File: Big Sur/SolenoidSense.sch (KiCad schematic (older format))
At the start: 12 parts, among them U4 ACS70331EOLCTR, U5 ACS70331EOLCTR, U6 ACS70331EOLCTR, U7 ACS70331EOLCTR, U8 ACS70331EOLCTR, U9 ACS70331EOLCTR

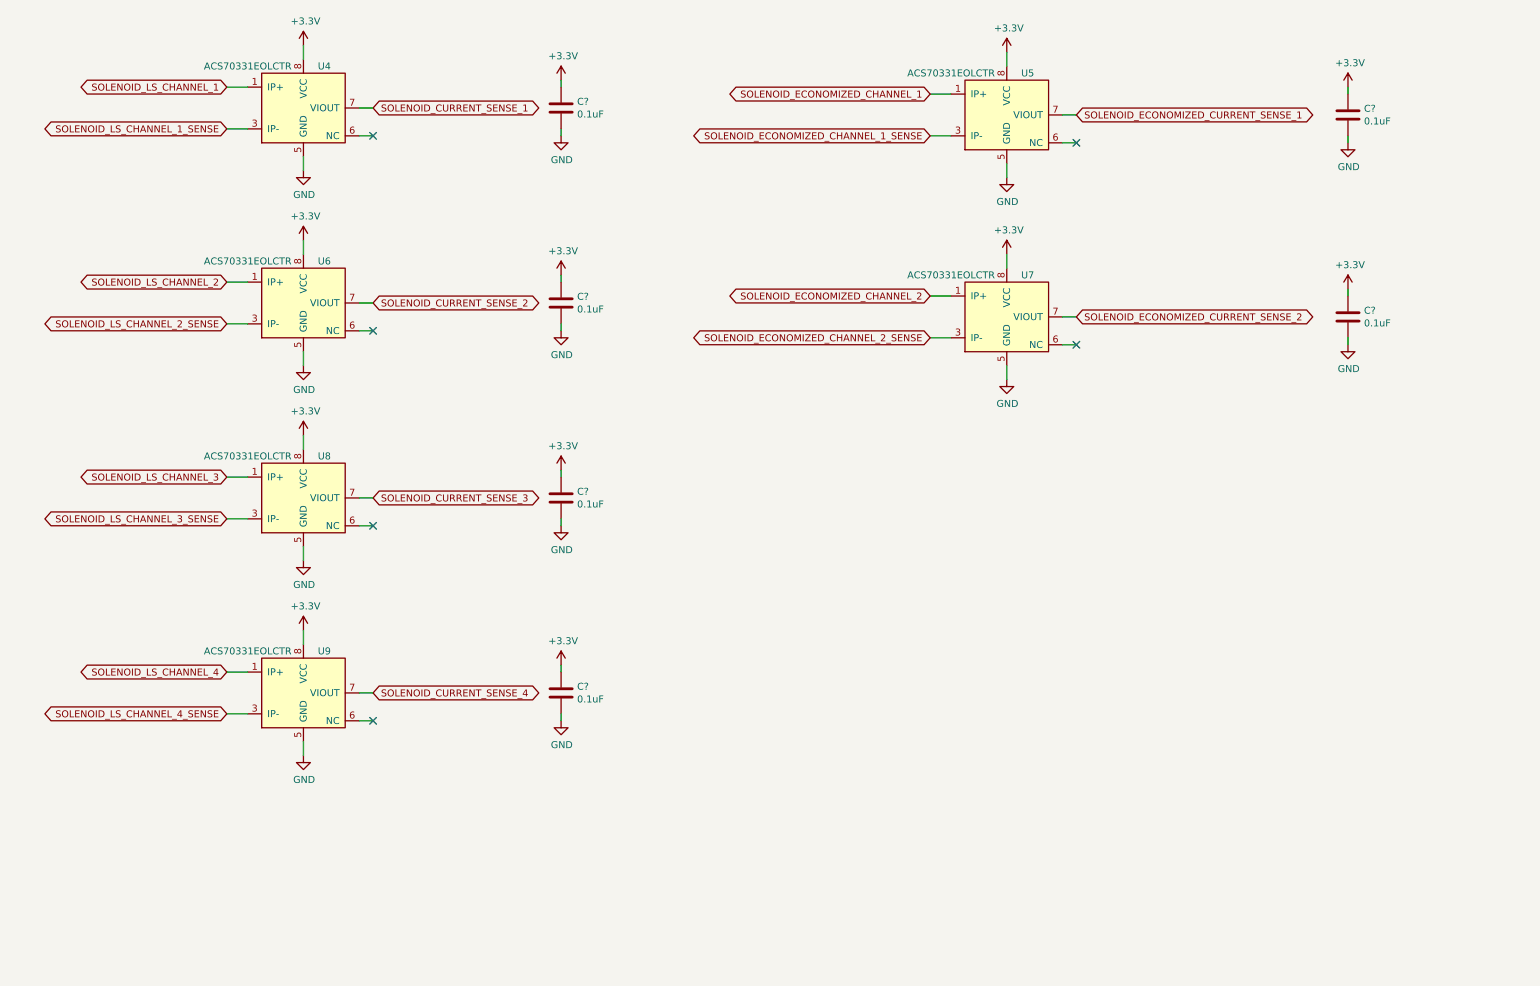
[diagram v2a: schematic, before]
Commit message: Schematics Complete
Still need to spec resistors, and XT30s, then should be ready for layout and routing.
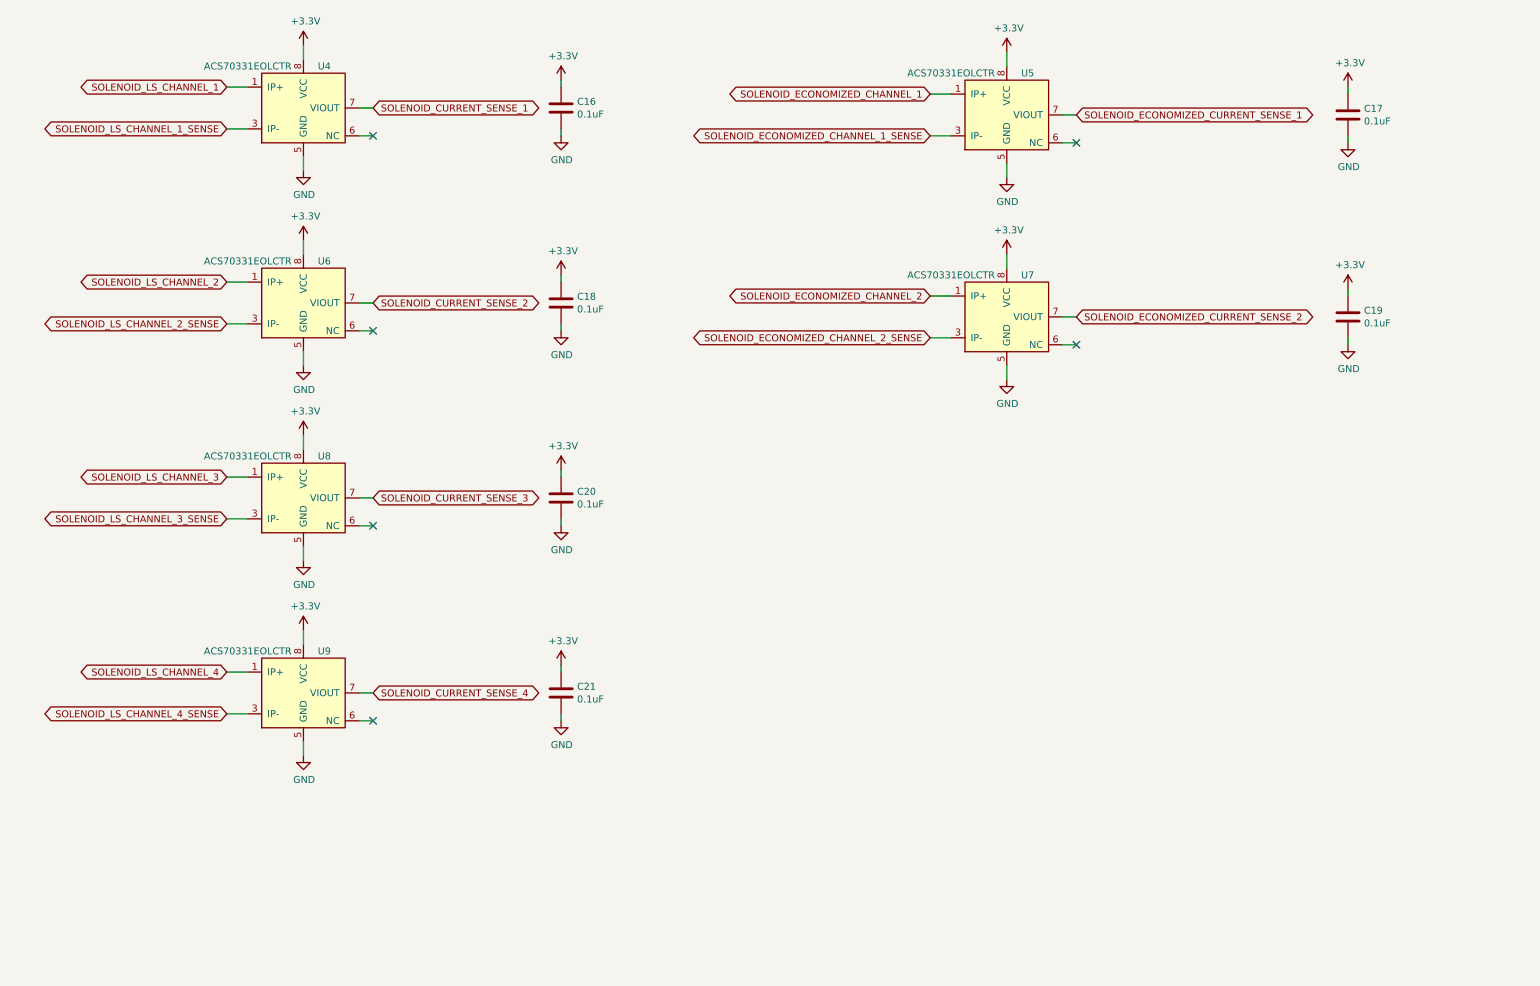
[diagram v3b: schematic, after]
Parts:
- gave numbers to parts that had none: 6
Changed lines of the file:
@@
 $EndDescr
 $Comp
-L power:+3.3V #PWR045
+L power:+3.3V #PWR046
 U 1 1 5DA28059
 P 2450 800
-F 0 "#PWR045" H 2450 650 50  0001 C CNN
+F 0 "#PWR046" H 2450 650 50  0001 C CNN
 F 1 "+3.3V" H 2465 973 50  0000 C CNN
 F 2 "" H 2450 800 50  0001 C CNN
@@
 	2450 900  2450 800
 $Comp
-L power:GND #PWR051
+L power:GND #PWR052
 U 1 1 5DA3AF60
 P 2450 1700
-F 0 "#PWR051" H 2450 1450 50  0001 C CNN
+F 0 "#PWR052" H 2450 1450 50  0001 C CNN
 F 1 "GND" H 2455 1527 50  0000 C CNN
 F 2 "" H 2450 1700 50  0001 C CNN
@@
 $EndComp
 $Comp
-L power:+3.3V #PWR047
+L power:+3.3V #PWR048
 U 1 1 5DA3EB08
 P 4300 1050
-F 0 "#PWR047" H 4300 900 50  0001 C CNN
+F 0 "#PWR048" H 4300 900 50  0001 C CNN
 F 1 "+3.3V" H 4315 1223 50  0000 C CNN
 F 2 "" H 4300 1050 50  0001 C CNN
@@
 $EndComp
 $Comp
-L power:GND #PWR049
+L power:GND #PWR050
 U 1 1 5DA3F02D
 P 4300 1450
-F 0 "#PWR049" H 4300 1200 50  0001 C CNN
+F 0 "#PWR050" H 4300 1200 50  0001 C CNN
 F 1 "GND" H 4305 1277 50  0000 C CNN
 F 2 "" H 4300 1450 50  0001 C CNN
@@
 SOLENOID_LS_CHANNEL_1
 $Comp
-L power:+3.3V #PWR053
+L power:+3.3V #PWR054
 U 1 1 5DC16BB4
 P 2450 2200
-F 0 "#PWR053" H 2450 2050 50  0001 C CNN
+F 0 "#PWR054" H 2450 2050 50  0001 C CNN
 F 1 "+3.3V" H 2465 2373 50  0000 C CNN
 F 2 "" H 2450 2200 50  0001 C CNN
@@
 	2450 2300 2450 2200
 $Comp
-L power:GND #PWR059
+L power:GND #PWR060
 U 1 1 5DC16BC0
 P 2450 3100
-F 0 "#PWR059" H 2450 2850 50  0001 C CNN
+F 0 "#PWR060" H 2450 2850 50  0001 C CNN
 F 1 "GND" H 2455 2927 50  0000 C CNN
 F 2 "" H 2450 3100 50  0001 C CNN
@@
 SOLENOID_LS_CHANNEL_2
 $Comp
-L power:+3.3V #PWR061
+L power:+3.3V #PWR062
 U 1 1 5DC1B95D
 P 2450 3600
-F 0 "#PWR061" H 2450 3450 50  0001 C CNN
+F 0 "#PWR062" H 2450 3450 50  0001 C CNN
 F 1 "+3.3V" H 2465 3773 50  0000 C CNN
 F 2 "" H 2450 3600 50  0001 C CNN
@@
 	2450 3700 2450 3600
 $Comp
-L power:GND #PWR064
+L power:GND #PWR065
 U 1 1 5DC1B969
 P 2450 4500
-F 0 "#PWR064" H 2450 4250 50  0001 C CNN
+F 0 "#PWR065" H 2450 4250 50  0001 C CNN
 F 1 "GND" H 2455 4327 50  0000 C CNN
 F 2 "" H 2450 4500 50  0001 C CNN
@@
 SOLENOID_LS_CHANNEL_3
 $Comp
-L power:+3.3V #PWR065
+L power:+3.3V #PWR066
 U 1 1 5DC1B9A8
 P 2450 5000
-F 0 "#PWR065" H 2450 4850 50  0001 C CNN
+F 0 "#PWR066" H 2450 4850 50  0001 C CNN
 F 1 "+3.3V" H 2465 5173 50  0000 C CNN
 F 2 "" H 2450 5000 50  0001 C CNN
@@
 	2450 5100 2450 5000
 $Comp
-L power:GND #PWR068
+L power:GND #PWR069
 U 1 1 5DC1B9B4
 P 2450 5900
-F 0 "#PWR068" H 2450 5650 50  0001 C CNN
+F 0 "#PWR069" H 2450 5650 50  0001 C CNN
 F 1 "GND" H 2455 5727 50  0000 C CNN
 F 2 "" H 2450 5900 50  0001 C CNN
@@
 SOLENOID_LS_CHANNEL_4
 $Comp
-L power:+3.3V #PWR046
+L power:+3.3V #PWR047
 U 1 1 5DC2E2F5
 P 7500 850
-F 0 "#PWR046" H 7500 700 50  0001 C CNN
+F 0 "#PWR047" H 7500 700 50  0001 C CNN
 F 1 "+3.3V" H 7515 1023 50  0000 C CNN
 F 2 "" H 7500 850 50  0001 C CNN
@@
 	7500 950  7500 850
 $Comp
-L power:GND #PWR052
+L power:GND #PWR053
 U 1 1 5DC2E301
 P 7500 1750
-F 0 "#PWR052" H 7500 1500 50  0001 C CNN
+F 0 "#PWR053" H 7500 1500 50  0001 C CNN
 F 1 "GND" H 7505 1577 50  0000 C CNN
 F 2 "" H 7500 1750 50  0001 C CNN
@@
 SOLENOID_ECONOMIZED_CHANNEL_1
 $Comp
-L power:+3.3V #PWR054
+L power:+3.3V #PWR055
 U 1 1 5DC2E340
 P 7500 2300
-F 0 "#PWR054" H 7500 2150 50  0001 C CNN
+F 0 "#PWR055" H 7500 2150 50  0001 C CNN
 F 1 "+3.3V" H 7515 2473 50  0000 C CNN
 F 2 "" H 7500 2300 50  0001 C CNN
@@
 	7500 2400 7500 2300
 $Comp
-L power:GND #PWR060
+L power:GND #PWR061
 U 1 1 5DC2E34C
 P 7500 3200
-F 0 "#PWR060" H 7500 2950 50  0001 C CNN
+F 0 "#PWR061" H 7500 2950 50  0001 C CNN
 F 1 "GND" H 7505 3027 50  0000 C CNN
 F 2 "" H 7500 3200 50  0001 C CNN
@@
 AR Path="/5D6EB2B2/5D99FB16" Ref="C?"  Part="1"
 AR Path="/5D71C3EA/5D99FB16" Ref="C?"  Part="1"
-AR Path="/5D765C4F/5D99FB16" Ref="C?"  Part="1"
-F 0 "C?" H 4415 1296 50  0000 L CNN
+AR Path="/5D765C4F/5D99FB16" Ref="C16"  Part="1"
+F 0 "C16" H 4415 1296 50  0000 L CNN
 F 1 "0.1uF" H 4415 1205 50  0000 L CNN
 F 2 "Capacitor_SMD:C_0603_1608Metric_Pad1.05x0.95mm_HandSolder" H 4300 1250 50  0001 C CNN
@@
 $EndComp
 $Comp
-L power:+3.3V #PWR?
+L power:+3.3V #PWR056
 U 1 1 5D9B00B3
 P 4300 2450
-F 0 "#PWR?" H 4300 2300 50  0001 C CNN
+F 0 "#PWR056" H 4300 2300 50  0001 C CNN
 F 1 "+3.3V" H 4315 2623 50  0000 C CNN
 F 2 "" H 4300 2450 50  0001 C CNN
@@
 $EndComp
 $Comp
-L power:GND #PWR?
+L power:GND #PWR058
 U 1 1 5D9B00B9
 P 4300 2850
-F 0 "#PWR?" H 4300 2600 50  0001 C CNN
+F 0 "#PWR058" H 4300 2600 50  0001 C CNN
 F 1 "GND" H 4305 2677 50  0000 C CNN
 F 2 "" H 4300 2850 50  0001 C CNN
@@
 AR Path="/5D6EB2B2/5D9B00C3" Ref="C?"  Part="1"
 AR Path="/5D71C3EA/5D9B00C3" Ref="C?"  Part="1"
-AR Path="/5D765C4F/5D9B00C3" Ref="C?"  Part="1"
-F 0 "C?" H 4415 2696 50  0000 L CNN
+AR Path="/5D765C4F/5D9B00C3" Ref="C18"  Part="1"
+F 0 "C18" H 4415 2696 50  0000 L CNN
 F 1 "0.1uF" H 4415 2605 50  0000 L CNN
 F 2 "Capacitor_SMD:C_0603_1608Metric_Pad1.05x0.95mm_HandSolder" H 4300 2650 50  0001 C CNN
@@
 $EndComp
 $Comp
-L power:+3.3V #PWR?
+L power:+3.3V #PWR063
 U 1 1 5D9B13C2
 P 4300 3850
-F 0 "#PWR?" H 4300 3700 50  0001 C CNN
+F 0 "#PWR063" H 4300 3700 50  0001 C CNN
 F 1 "+3.3V" H 4315 4023 50  0000 C CNN
 F 2 "" H 4300 3850 50  0001 C CNN
@@
 $EndComp
 $Comp
-L power:GND #PWR?
+L power:GND #PWR064
 U 1 1 5D9B13C8
 P 4300 4250
-F 0 "#PWR?" H 4300 4000 50  0001 C CNN
+F 0 "#PWR064" H 4300 4000 50  0001 C CNN
 F 1 "GND" H 4305 4077 50  0000 C CNN
 F 2 "" H 4300 4250 50  0001 C CNN
@@
 AR Path="/5D6EB2B2/5D9B13D2" Ref="C?"  Part="1"
 AR Path="/5D71C3EA/5D9B13D2" Ref="C?"  Part="1"
-AR Path="/5D765C4F/5D9B13D2" Ref="C?"  Part="1"
-F 0 "C?" H 4415 4096 50  0000 L CNN
+AR Path="/5D765C4F/5D9B13D2" Ref="C20"  Part="1"
+F 0 "C20" H 4415 4096 50  0000 L CNN
 F 1 "0.1uF" H 4415 4005 50  0000 L CNN
 F 2 "Capacitor_SMD:C_0603_1608Metric_Pad1.05x0.95mm_HandSolder" H 4300 4050 50  0001 C CNN
@@
 $EndComp
 $Comp
-L power:+3.3V #PWR?
+L power:+3.3V #PWR067
 U 1 1 5D9B2921
 P 4300 5250
-F 0 "#PWR?" H 4300 5100 50  0001 C CNN
+F 0 "#PWR067" H 4300 5100 50  0001 C CNN
 F 1 "+3.3V" H 4315 5423 50  0000 C CNN
 F 2 "" H 4300 5250 50  0001 C CNN
@@
 $EndComp
 $Comp
-L power:GND #PWR?
+L power:GND #PWR068
 U 1 1 5D9B2927
 P 4300 5650
-F 0 "#PWR?" H 4300 5400 50  0001 C CNN
+F 0 "#PWR068" H 4300 5400 50  0001 C CNN
 F 1 "GND" H 4305 5477 50  0000 C CNN
 F 2 "" H 4300 5650 50  0001 C CNN
@@
 AR Path="/5D6EB2B2/5D9B2931" Ref="C?"  Part="1"
 AR Path="/5D71C3EA/5D9B2931" Ref="C?"  Part="1"
-AR Path="/5D765C4F/5D9B2931" Ref="C?"  Part="1"
-F 0 "C?" H 4415 5496 50  0000 L CNN
+AR Path="/5D765C4F/5D9B2931" Ref="C21"  Part="1"
+F 0 "C21" H 4415 5496 50  0000 L CNN
 F 1 "0.1uF" H 4415 5405 50  0000 L CNN
 F 2 "Capacitor_SMD:C_0603_1608Metric_Pad1.05x0.95mm_HandSolder" H 4300 5450 50  0001 C CNN
@@
 $EndComp
 $Comp
-L power:+3.3V #PWR?
+L power:+3.3V #PWR049
 U 1 1 5D9BC089
 P 9950 1100
-F 0 "#PWR?" H 9950 950 50  0001 C CNN
+F 0 "#PWR049" H 9950 950 50  0001 C CNN
 F 1 "+3.3V" H 9965 1273 50  0000 C CNN
 F 2 "" H 9950 1100 50  0001 C CNN
@@
 $EndComp
 $Comp
-L power:GND #PWR?
+L power:GND #PWR051
 U 1 1 5D9BC093
 P 9950 1500
-F 0 "#PWR?" H 9950 1250 50  0001 C CNN
+F 0 "#PWR051" H 9950 1250 50  0001 C CNN
 F 1 "GND" H 9955 1327 50  0000 C CNN
 F 2 "" H 9950 1500 50  0001 C CNN
@@
 AR Path="/5D6EB2B2/5D9BC0A1" Ref="C?"  Part="1"
 AR Path="/5D71C3EA/5D9BC0A1" Ref="C?"  Part="1"
-AR Path="/5D765C4F/5D9BC0A1" Ref="C?"  Part="1"
-F 0 "C?" H 10065 1346 50  0000 L CNN
+AR Path="/5D765C4F/5D9BC0A1" Ref="C17"  Part="1"
+F 0 "C17" H 10065 1346 50  0000 L CNN
 F 1 "0.1uF" H 10065 1255 50  0000 L CNN
 F 2 "Capacitor_SMD:C_0603_1608Metric_Pad1.05x0.95mm_HandSolder" H 9950 1300 50  0001 C CNN
@@
 $EndComp
 $Comp
-L power:+3.3V #PWR?
+L power:+3.3V #PWR057
 U 1 1 5D9BC0AB
 P 9950 2550
-F 0 "#PWR?" H 9950 2400 50  0001 C CNN
+F 0 "#PWR057" H 9950 2400 50  0001 C CNN
 F 1 "+3.3V" H 9965 2723 50  0000 C CNN
 F 2 "" H 9950 2550 50  0001 C CNN
@@
 $EndComp
 $Comp
-L power:GND #PWR?
+L power:GND #PWR059
 U 1 1 5D9BC0B5
 P 9950 2950
-F 0 "#PWR?" H 9950 2700 50  0001 C CNN
+F 0 "#PWR059" H 9950 2700 50  0001 C CNN
 F 1 "GND" H 9955 2777 50  0000 C CNN
 F 2 "" H 9950 2950 50  0001 C CNN
@@
 AR Path="/5D6EB2B2/5D9BC0C3" Ref="C?"  Part="1"
 AR Path="/5D71C3EA/5D9BC0C3" Ref="C?"  Part="1"
-AR Path="/5D765C4F/5D9BC0C3" Ref="C?"  Part="1"
-F 0 "C?" H 10065 2796 50  0000 L CNN
+AR Path="/5D765C4F/5D9BC0C3" Ref="C19"  Part="1"
+F 0 "C19" H 10065 2796 50  0000 L CNN
 F 1 "0.1uF" H 10065 2705 50  0000 L CNN
 F 2 "Capacitor_SMD:C_0603_1608Metric_Pad1.05x0.95mm_HandSolder" H 9950 2750 50  0001 C CNN
